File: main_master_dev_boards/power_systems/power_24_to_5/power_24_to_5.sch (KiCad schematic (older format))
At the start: 36 parts, among them J1 Switch_in, J10 5_in, J2 24_in, J3 GND_in, J4 PGoodMain_out, J5 ref_out, J6 5_out, J7 GND_out, J8 3v3_out, J9 PGoodBackup_out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

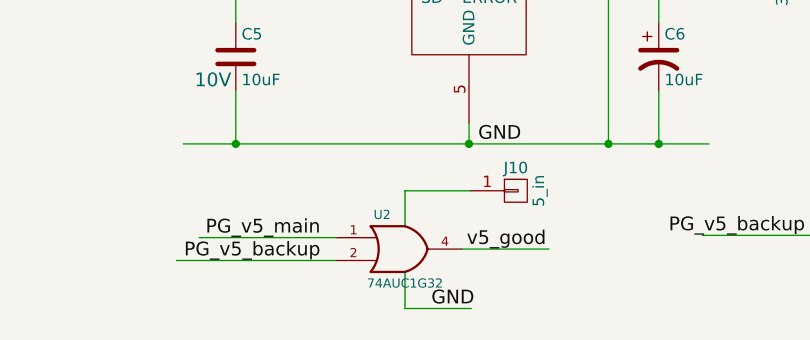
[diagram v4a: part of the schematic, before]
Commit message: Added correct caps for buck and LDO. Changed the or gate to 5V tollerant variant
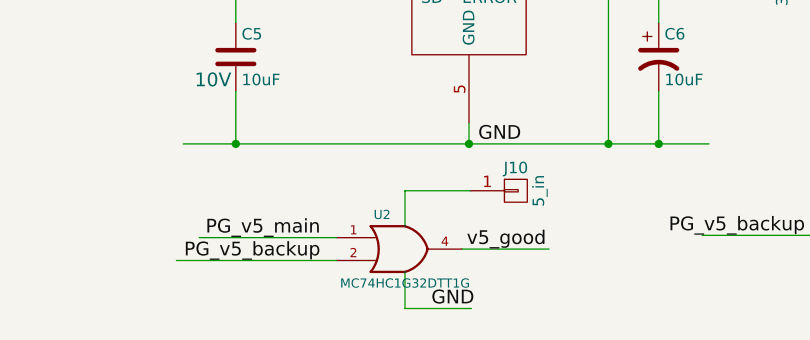
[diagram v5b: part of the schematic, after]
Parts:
- C1, C3: Field5 C1005X5R1V225K050BC -> (none); Resistance 5.92mOhms -> (none)
- C4, C8: footprint Capacitors_SMD:C_0805_HandSoldering -> Capacitors_SMD:C_2220_HandSoldering; Field5 C2012X5R1A336M125AC -> (none); Resistance 1.69mOhms -> (none)
- U2: value 74AUC1G32 -> MC74HC1G32DTT1G
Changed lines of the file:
@@
 F 1 "2.2uF" H 1970 2580 50  0000 L CNN
 F 2 "Capacitors_SMD:C_0805_HandSoldering" H 1795 2850 50  0001 C CNN
-F 3 "" H 1945 2680 50  0001 C CNN
-F 4 "5.92mOhms" H 1645 2580 60  0001 C CNN "Resistance"
-F 5 "C1005X5R1V225K050BC" H 1945 2680 60  0001 C CNN "Field5"
+F 3 "https://www.digikey.com/product-detail/en/C2012X7R1H225K125AC/445-5968-1-ND/2444009" H 1945 2680 50  0001 C CNN
 	1    1945 2680
 	1    0    0    -1
@@
 F 1 "8.2uH" V 5925 2350 50  0000 C CNN
 F 2 "Bourns:Bourns-SRP7028A" H 5850 2350 50  0001 C CNN
-F 3 "" H 5850 2350 50  0000 C CNN
+F 3 "https://www.digikey.com/product-detail/en/SRP7028A-8R2M/SRP7028A-8R2MCT-ND/4876743" H 5850 2350 50  0001 C CNN
 	1    5850 2350
 	0    1    1    0
@@
 F 1 "10uF" H 4855 5085 50  0000 L CNN
 F 2 "Capacitors_SMD:C_0805_HandSoldering" H 4868 5035 50  0001 C CNN
-F 3 "" H 4830 5185 50  0000 C CNN
+F 3 "https://www.digikey.com/product-detail/en/0805ZD106KAT2A/478-5167-1-ND/1913257" H 4830 5185 50  0001 C CNN
 F 4 "10V" H 4730 5085 60  0000 C CNN "Voltage"
 	1    4830 5185
@@
 F 1 "10uF" H 6705 5085 50  0000 L CNN
 F 2 "Capacitors_SMD:C_0805_HandSoldering" H 6680 5185 50  0001 C CNN
-F 3 "" H 6680 5185 50  0000 C CNN
+F 3 "https://www.digikey.com/product-detail/en/0805ZD106KAT2A/478-5167-1-ND/1913257" H 6680 5185 50  0001 C CNN
 	1    6680 5185
 	1    0    0    -1
@@
 P 5570 6025
 F 0 "U2" H 5470 6175 40  0000 C CNN
-F 1 "74AUC1G32" H 5570 5875 40  0000 C CNN
+F 1 "MC74HC1G32DTT1G" H 5570 5875 40  0000 C CNN
 F 2 "TO_SOT_Packages_SMD:SOT-23-5_HandSoldering" H 5570 6025 60  0001 C CNN
-F 3 "https://octopart.com/sn74auc1g32dckr-texas+instruments-464483" H 5570 6025 60  0001 C CNN
+F 3 "https://www.digikey.com/product-detail/en/MC74HC1G32DTT1G/MC74HC1G32DTT1GOSCT-ND/1967106" H 5570 6025 60  0001 C CNN
 	1    5570 6025
 	1    0    0    -1
@@
 F 0 "C4" H 6445 2790 50  0000 L CNN
 F 1 "47uF X7R" H 6445 2590 50  0000 L CNN
-F 2 "Capacitors_SMD:C_0805_HandSoldering" H 6320 2740 50  0001 C CNN
-F 3 "" H 6420 2690 50  0000 C CNN
-F 4 "1.69mOhms" H 6620 2490 60  0001 C CNN "Resistance"
-F 5 "C2012X5R1A336M125AC" H 6420 2690 60  0001 C CNN "Field5"
+F 2 "Capacitors_SMD:C_2220_HandSoldering" H 6320 2740 50  0001 C CNN
+F 3 "https://www.digikey.com/product-detail/en/CGA9N3X7R1C476M230KB/445-7935-1-ND/2781439" H 6420 2690 50  0001 C CNN
 	1    6420 2690
 	1    0    0    1
@@
 F 0 "C8" H 6155 2785 50  0000 L CNN
 F 1 "47uF X7R" H 5925 2595 50  0000 L CNN
-F 2 "Capacitors_SMD:C_0805_HandSoldering" H 6030 2735 50  0001 C CNN
-F 3 "" H 6130 2685 50  0000 C CNN
-F 4 "1.69mOhms" H 6330 2485 60  0001 C CNN "Resistance"
-F 5 "C2012X5R1A336M125AC" H 6130 2685 60  0001 C CNN "Field5"
+F 2 "Capacitors_SMD:C_2220_HandSoldering" H 6030 2735 50  0001 C CNN
+F 3 "https://www.digikey.com/product-detail/en/CGA9N3X7R1C476M230KB/445-7935-1-ND/2781439" H 6130 2685 50  0001 C CNN
 	1    6130 2685
 	1    0    0    -1
@@
 F 1 "2.2uF" H 2225 2580 50  0000 L CNN
 F 2 "Capacitors_SMD:C_0805_HandSoldering" H 2050 2850 50  0001 C CNN
-F 3 "" H 2200 2680 50  0001 C CNN
-F 4 "5.92mOhms" H 1900 2580 60  0001 C CNN "Resistance"
-F 5 "C1005X5R1V225K050BC" H 2200 2680 60  0001 C CNN "Field5"
+F 3 "https://www.digikey.com/product-detail/en/C2012X7R1H225K125AC/445-5968-1-ND/2444009" H 2200 2680 50  0001 C CNN
 	1    2200 2680
 	1    0    0    -1
